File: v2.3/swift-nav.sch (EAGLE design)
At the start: 149 parts, among them J1 SMA_EDGE, J6 ZX62-B-5PA, Q1 IRLML6401, U1 6SLX9FTG256, U10 MAX2769, U12 PT7M8206B33TA5EX, U13 M25PX80, U2 LTC3407A_DFN, U3 STM32-M-64-LQFP, U4 7Q-16.368MBG-T, U5 SMA_PATCH_SMDGND, U6 93LC56BT-I/OT, U7 FT232HQ, U8 B4050, U9 XC2401, X3 FPGA DEBUG, X4 NX5032GA-12M, X5 CONN_5-2

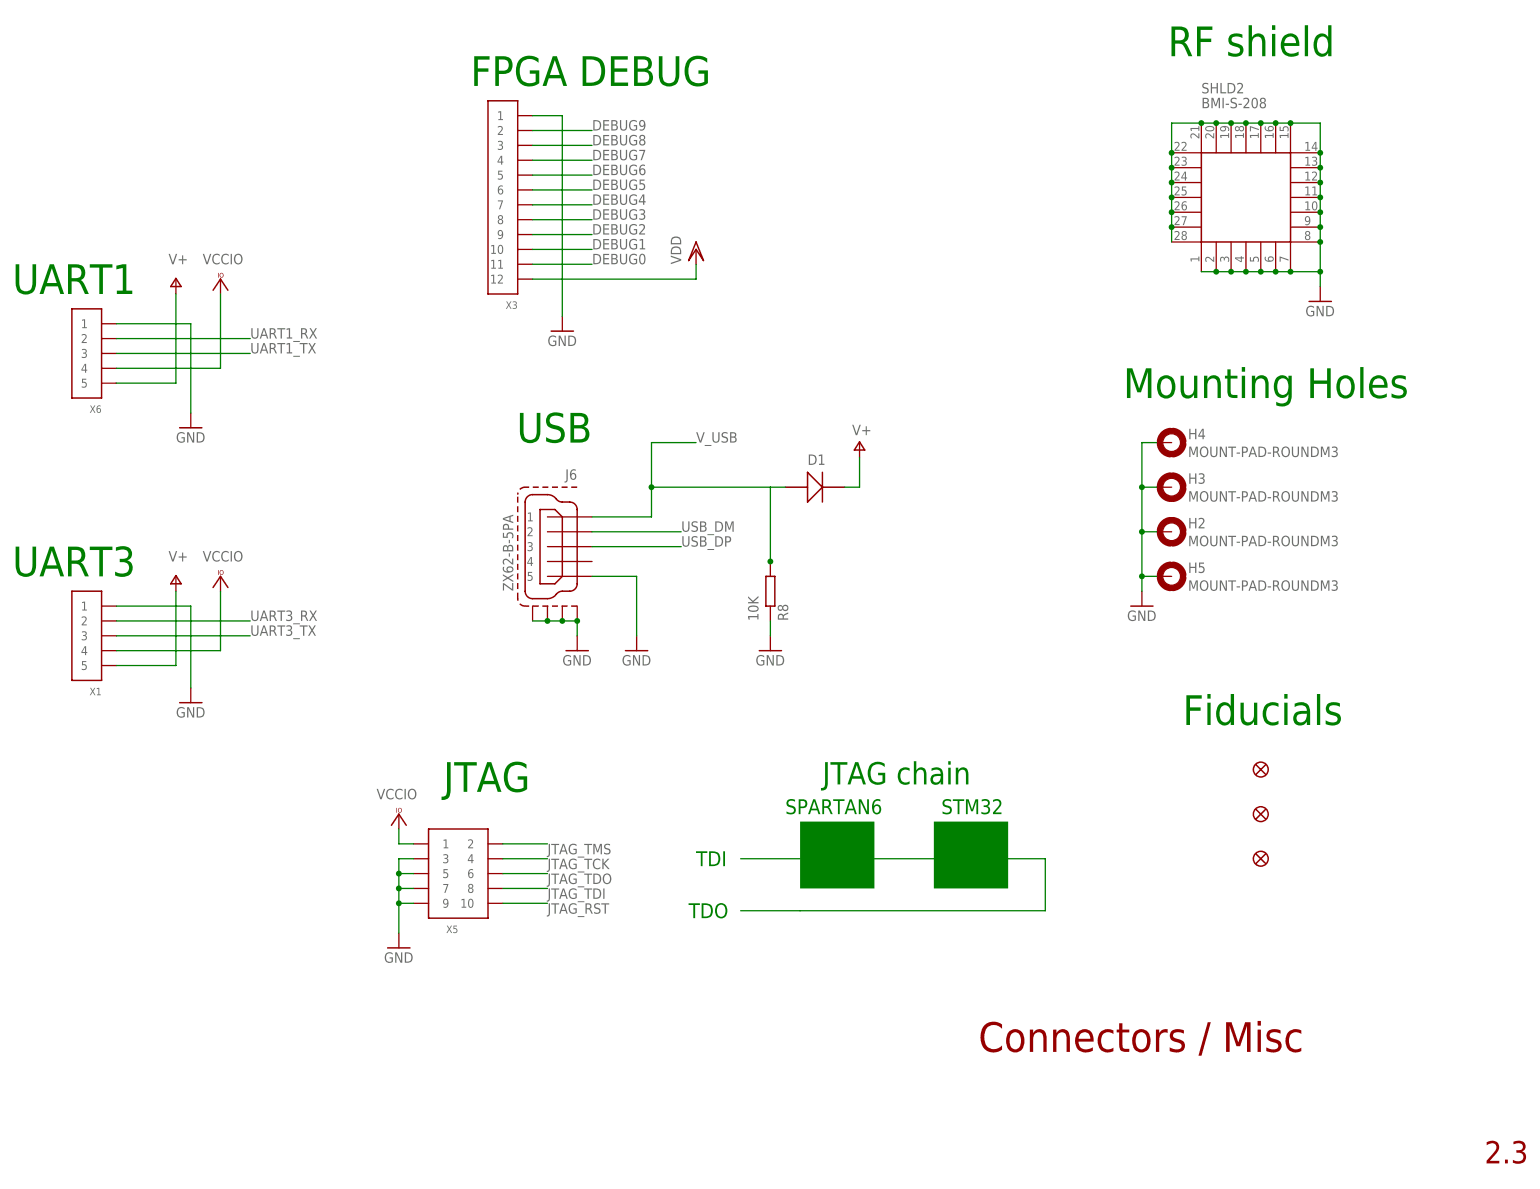
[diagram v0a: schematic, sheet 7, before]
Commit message: Debug connector was connected to VDD instead of V+ (post instead of pre-reverse polarity protection)
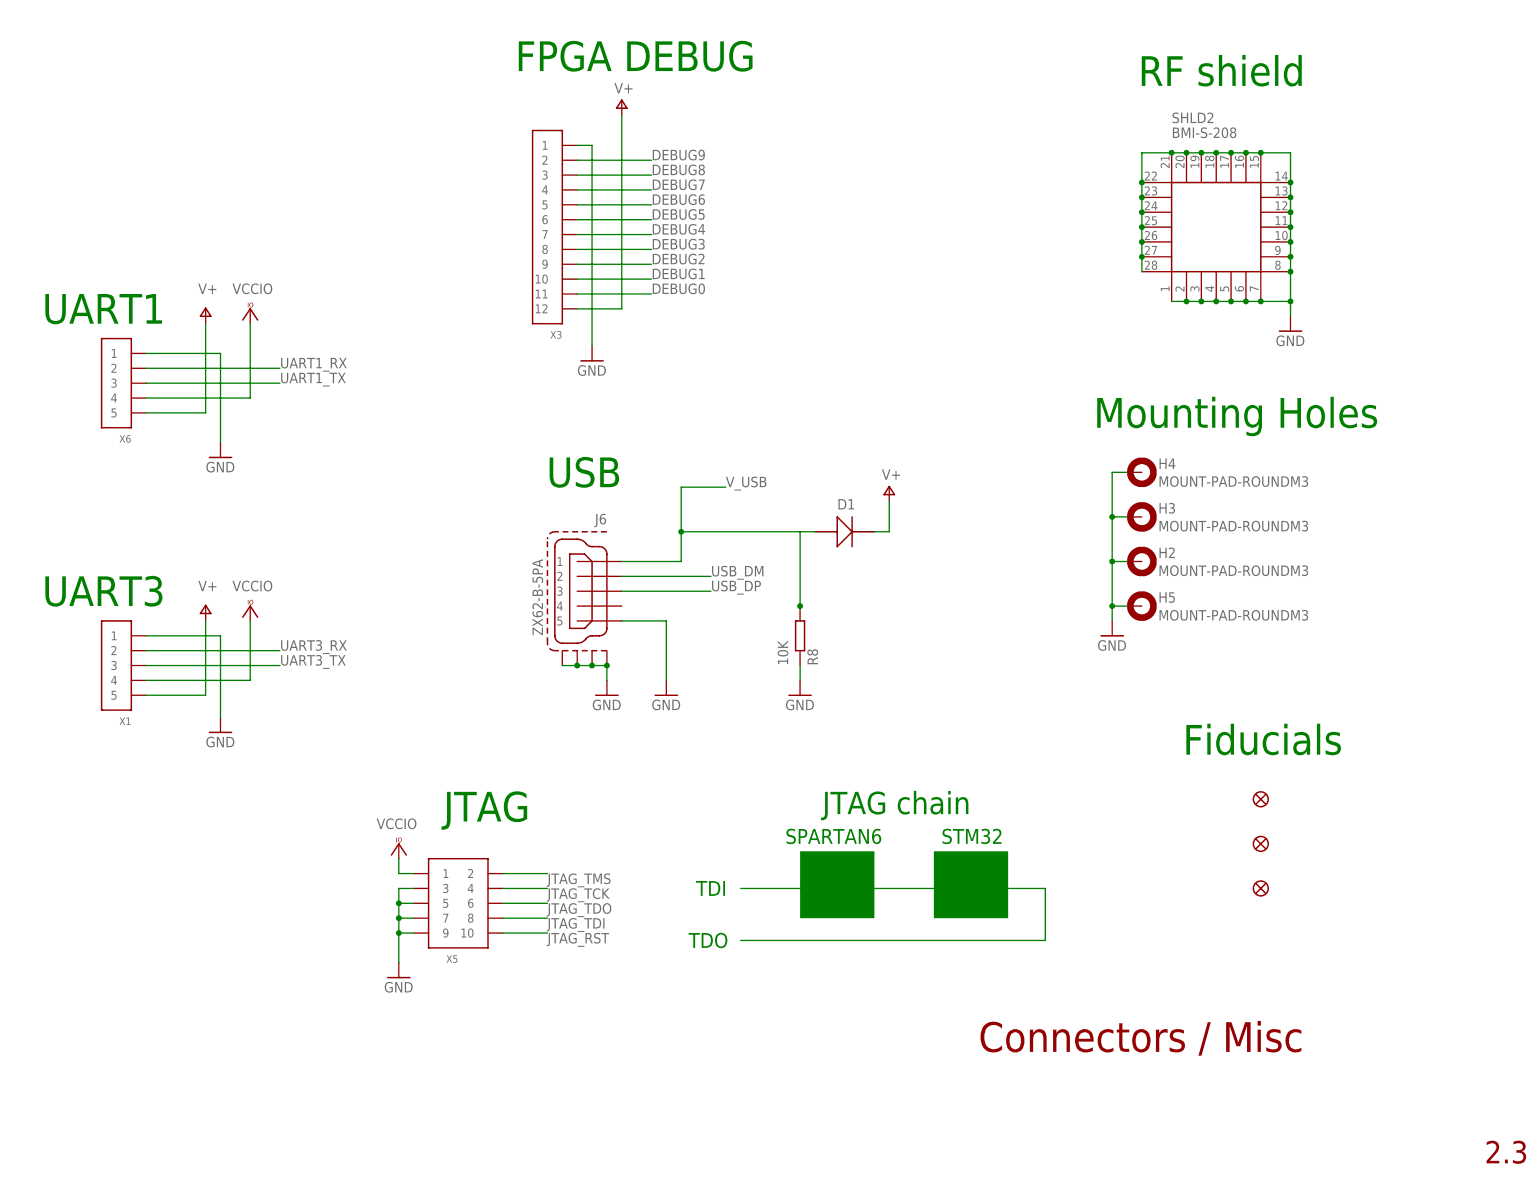
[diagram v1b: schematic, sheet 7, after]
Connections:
- net V+: now also X3.12
- net VDD: no longer X3.12
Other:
- moved on the sheet: D1, H2, H3, H4, H5, J6, R8, SHLD2, X1, X3, X5, X6

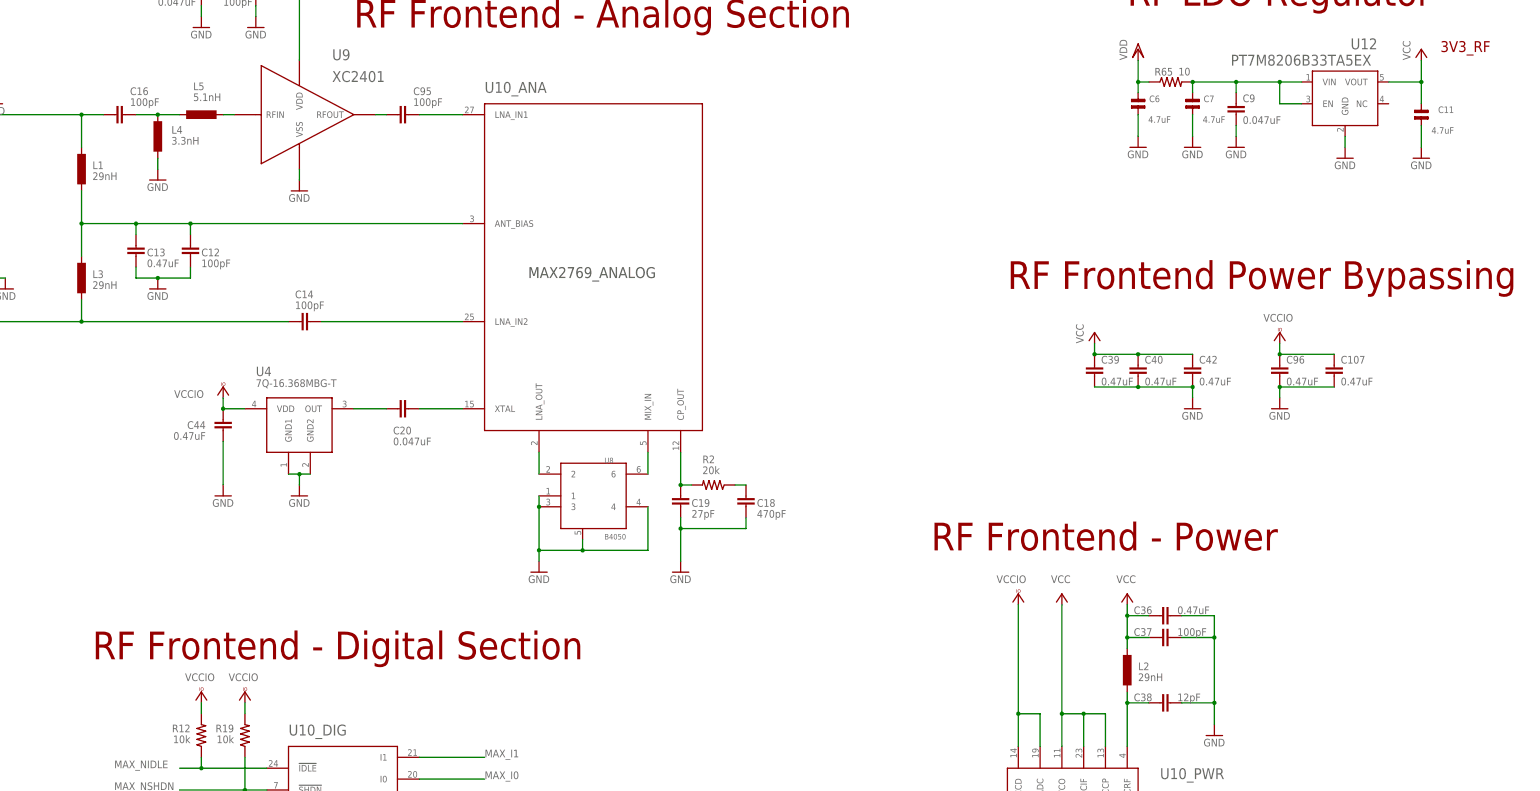
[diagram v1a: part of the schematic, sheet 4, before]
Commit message: Changed cap footprints to smaller versions
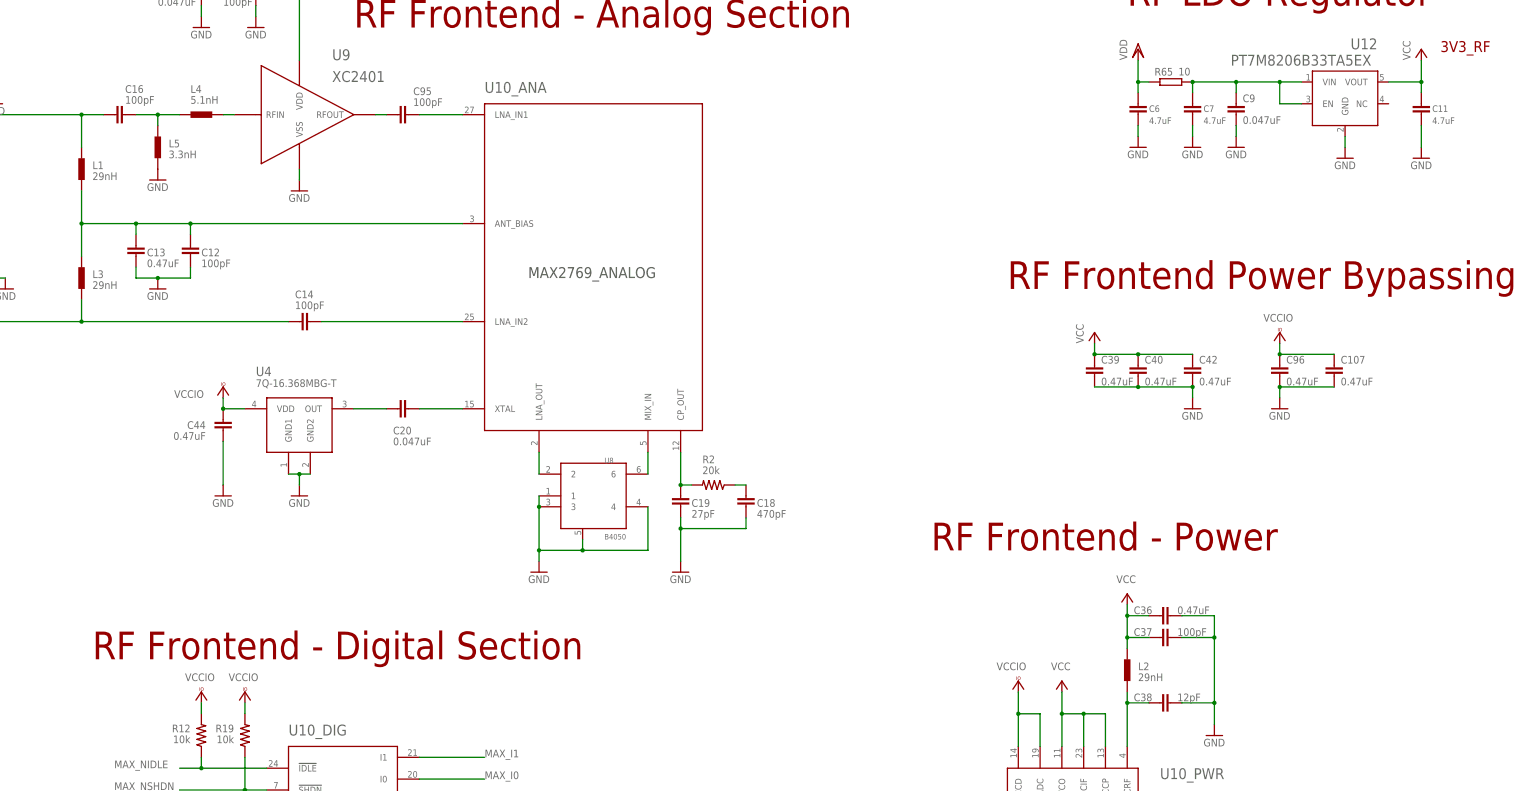
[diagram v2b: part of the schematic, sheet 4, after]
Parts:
- C1, C107, C12, C13, C14, C15, C16, C22, C23, C27, C31, C32, C34, C35, C36, C37, C38, C39, C40, C42, C47, C48, C49, C5, C52, C53, C54, C55, C62, C63, C66, C67, C72, C73, C75, C77, C82, C9, C95, C96: device rcl:C-EUC0402 -> pel_dipol_comp:CAPACITOR-0402
- C10, C17, C28, C29, C30, C33, C50, C51, C57, C59, C60, C61, C65, C71, C76, C8: device rcl:C-EUC0603K -> pel_dipol_comp:CAPACITOR-0603
- C11, C6, C7: device capsmd:C0603 -> pel_dipol_comp:CAPACITOR-0603
- C2, C3, C4: device rcl:C-USC1206 -> pel_dipol_comp:CAPACITOR-1206
- C21, C24, C25, C26, C86, C87: device rcl:C-EUC1210K -> rcl:C-EUC1210
- C56, C58, C64, C68, C70, C74: device rcl:C-EUC0603K -> pel_dipol_comp:CAPACITOR-0402
- L10, L11: device rcl:R-EU_R0805 -> pel_dipol_comp:INDUCTOR-0805
- L4: value 3.3nH -> 5.1nH
- L5: value 5.1nH -> 3.3nH
- LED1, LED2: device led:LEDCHIP-LED0603 -> pel_dipol_comp:LED-0603
- R1, R13, R14, R15, R16, R17, R18, R61, R62, R63, R64, R65: device rcl:R-US_R0402 -> pel_dipol_comp:RESISTOR-0402
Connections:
- new net N$1: X3.12
- net GND: now also L5.1; no longer L4.1
- net N$2: now also L4.2; no longer L5.1
- net N$35: now also L4.1; no longer L4.2
- net V+: no longer X3.12
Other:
- moved on the sheet: L4, L5

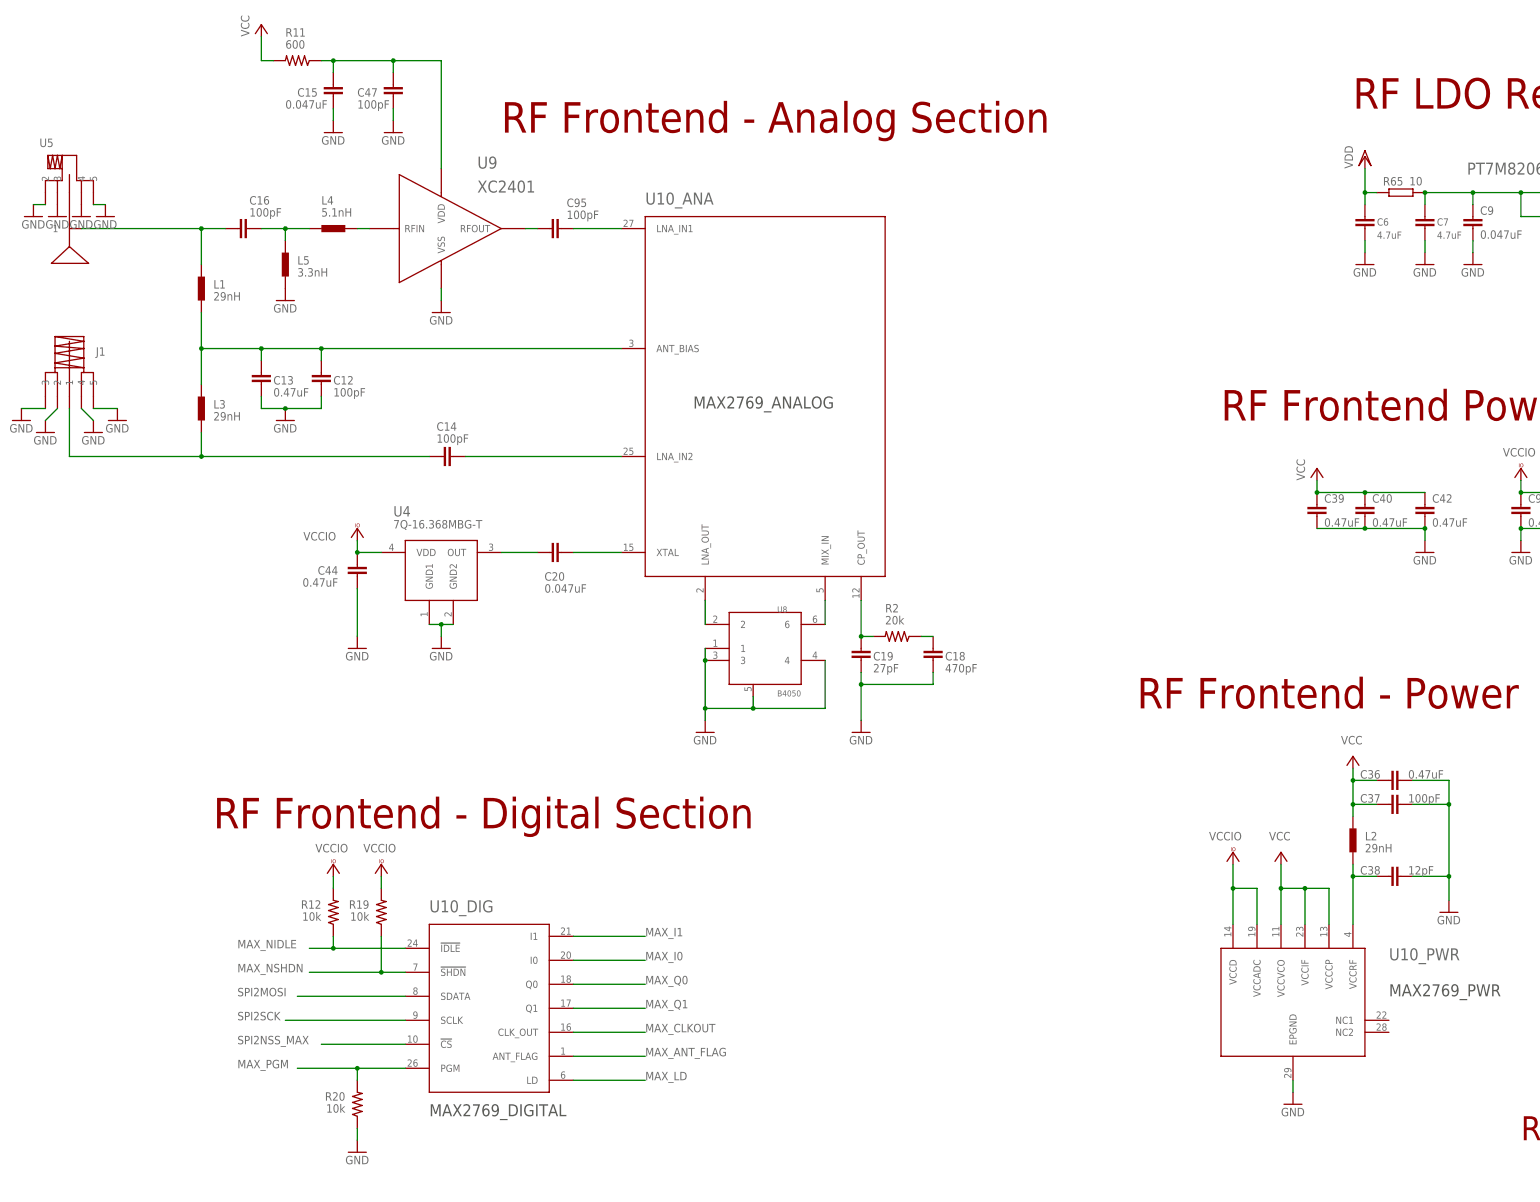
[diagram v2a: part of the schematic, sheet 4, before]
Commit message: Finished placing all components on board
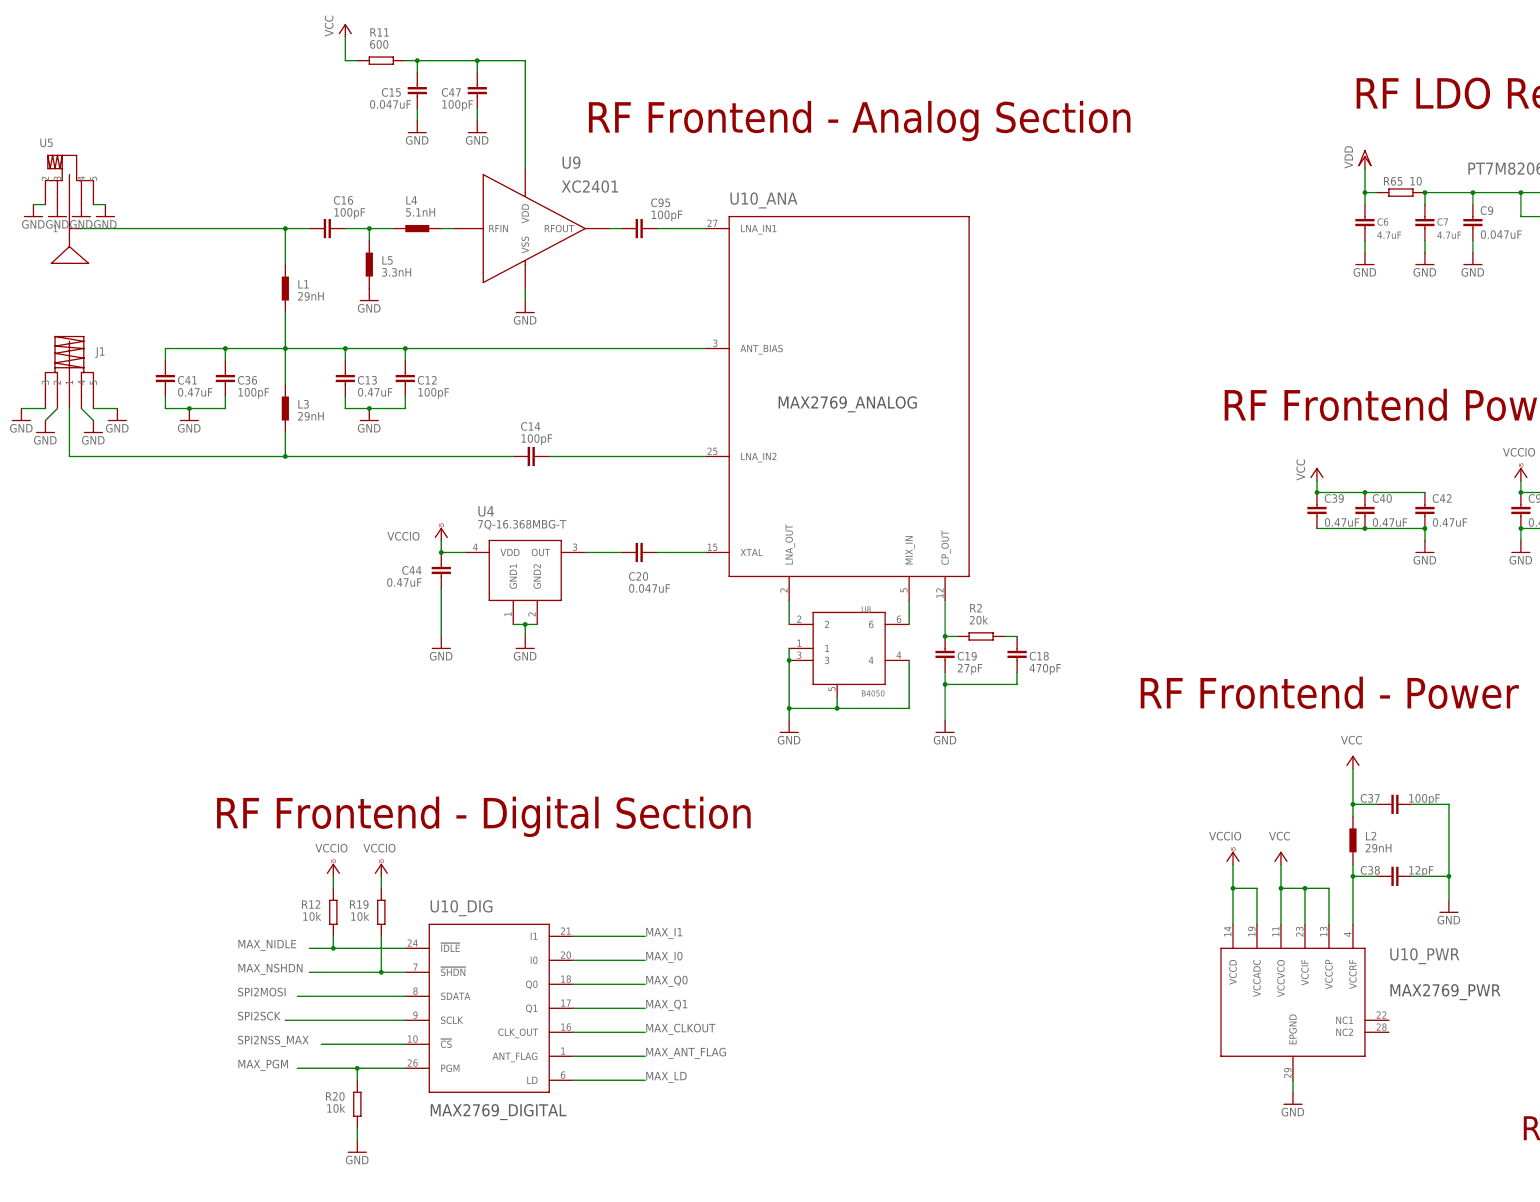
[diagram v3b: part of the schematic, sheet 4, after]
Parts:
- added C41: 0.47uF, pel_dipol_comp:CAPACITOR-0402
- C18, C19, C20, C44: device rcl:C-EUC0402 -> pel_dipol_comp:CAPACITOR-0402
- C36: value 0.47uF -> 100pF
- R11, R12, R19, R2, R20: device rcl:R-US_R0402 -> pel_dipol_comp:RESISTOR-0402
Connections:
- removed net N$37: C12.2, C13.2, L1.1, L3.2, U10_ANA.ANT_BIAS
- new net N$10: C12.2, C13.2, C36.2, C41.2, L1.1, L3.2, U10_ANA.ANT_BIAS
- net GND: now also C36.1, C41.1; no longer C36.2
- net VCC: no longer C36.1
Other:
- moved on the sheet: C12, C13, C14, C15, C16, C18, C19, C20, C36, C44, C47, C95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
